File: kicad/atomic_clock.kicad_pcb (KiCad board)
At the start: 2 copper layers, 282.9 x 44.2 mm, 78 parts, among them J1 Conn_02x05_Top_Bottom, J10 Conn_02x05_Top_Bottom, J11 Conn_02x05_Top_Bottom, J12 USB_B_Micro, J13 Conn_ARM_JTAG_SWD_10, J14 Conn_01x03_Female, J2 Conn_02x05_Top_Bottom, J3 Conn_02x05_Top_Bottom, J4 Conn_02x05_Top_Bottom, J5 USB_B_Micro, J6 Conn_02x05_Top_Bottom, J7 Conn_02x05_Top_Bottom, J8 Conn_02x05_Top_Bottom, J9 Conn_02x05_Top_Bottom, Q1 Q_Dual_PMOS, Q2 Q_Dual_PMOS, SW1 SW_Push, U1 D198K, U10 ATSAMDA1E16B-A, U11 D198K, U12 D198K, U13 D198K, U14 D198K, U15 D198K, U16 MAX7221xWG, U17 D198K, U18 D198K, U19 D198K, U2 D198K, U20 NCP1117LPST33T3G, U21 mems_osc_st1630, U22 DHT20, U23 DCF77, U24 MCP73831-2-OT, U25 TXB0101, U3 D198K, U4 D198K, U5 MAX7221xWG, U6 D198K, U7 D198K, U8 D198K, U9 D198K

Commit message: Added silkscreen commentary
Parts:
- moved BT1 11.6 mm to (196.9, 110.4)
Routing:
- net Net-(BT1-Pad1): track 115.7 -> 157.1 mm
- net GND: track 489.2 -> 477.6 mm
- net /1A2: track 154.0 -> 156.3 mm
- net /DCF_PDN: track 157.8 -> 159.6 mm
- net /1B2: track 154.0 -> 154.9 mm
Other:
- board text added: "Batt full Charging"
- board text added: "DCF77 Radio controlled clock v1.0, June 2022 Erik van Zijst <erik.van.zijst@gmail.com> github.com/erikvanzijst/radioclock"
- board text added: "◯ ◉"

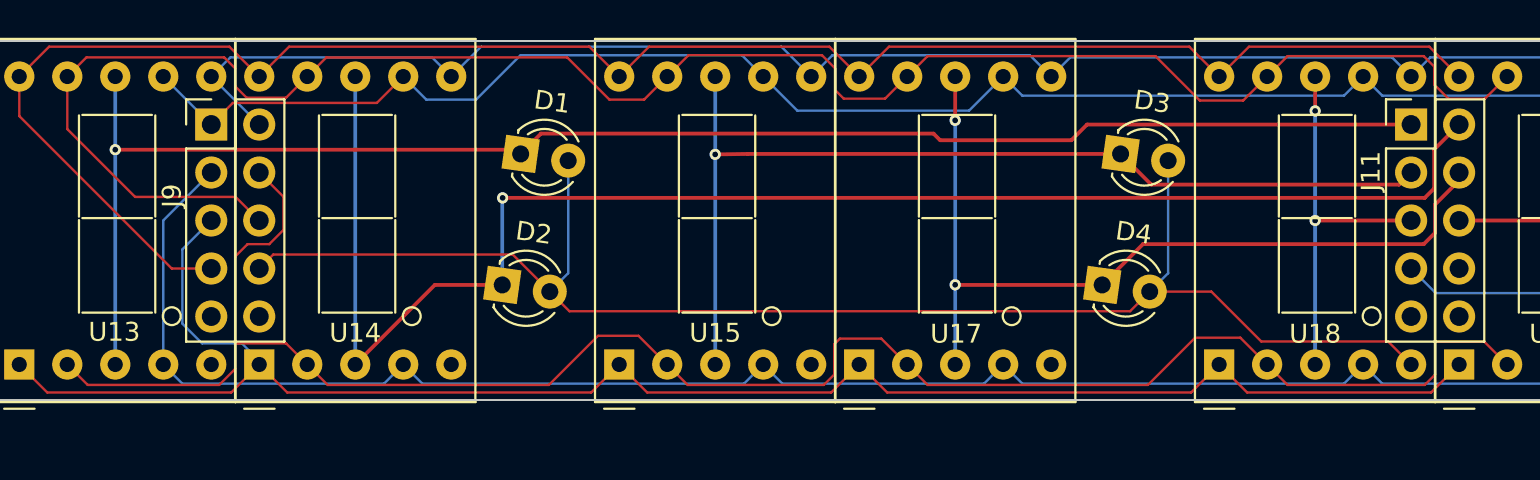
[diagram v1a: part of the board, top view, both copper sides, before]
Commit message: Switched flat top LEDs
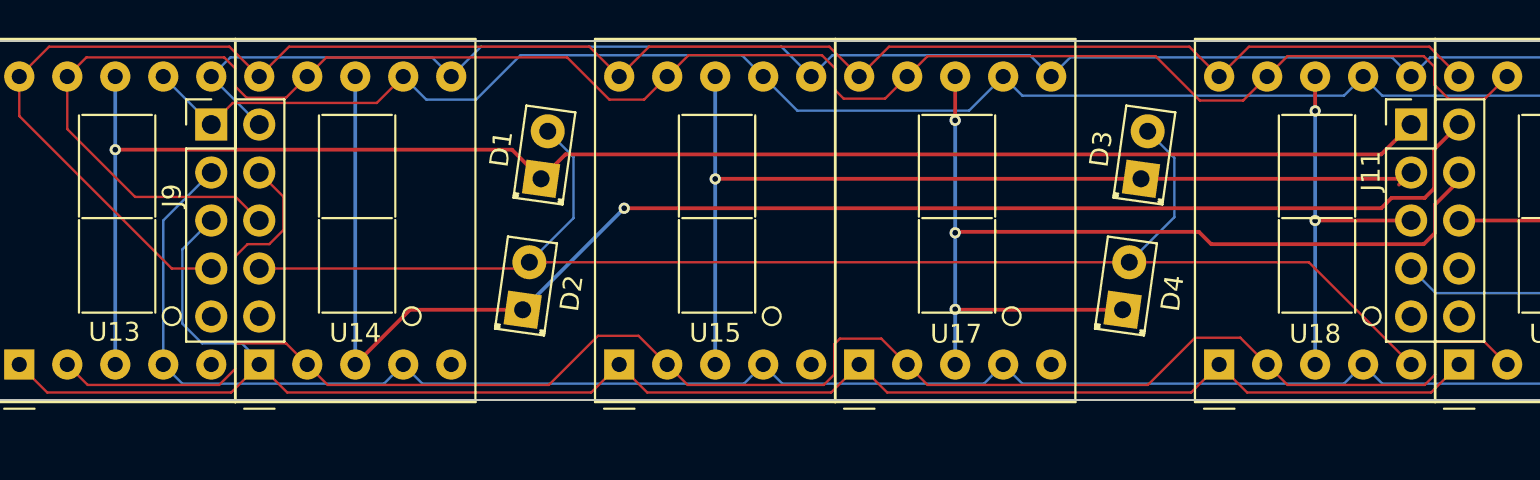
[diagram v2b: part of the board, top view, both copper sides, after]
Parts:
- D1, D2, D3, D4: footprint LED_THT:LED_D3.0mm_FlatTop -> local_footprints:LED_D2.0mm_W4.8mm_H2.5mm_FlatTop
- moved D3 1.26 mm to (277.5, 87.5), turned to 82 degrees
- moved D1 1.26 mm to (245.8, 87.5), turned to 82 degrees
- moved D2 1.26 mm to (244.8, 94.4), turned to 82 degrees
- moved D4 1.26 mm to (276.6, 94.4), turned to 82 degrees
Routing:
- net /3s13: track 45.5 -> 53.8 mm, vias 2 -> 3
- net /3s11: track 82.8 -> 80.1 mm
- net /3DP2: track 79.2 -> 80.3 mm
- net /3s10: track 84.8 -> 85.6 mm

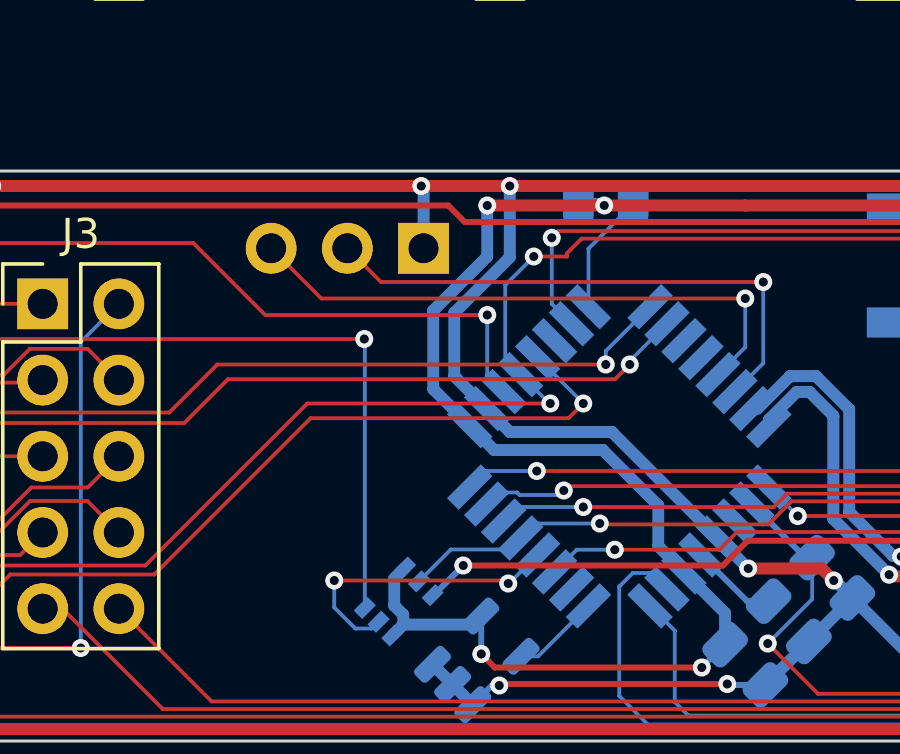
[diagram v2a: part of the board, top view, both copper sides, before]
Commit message: Placed and routed decoupling cap on VDDANA
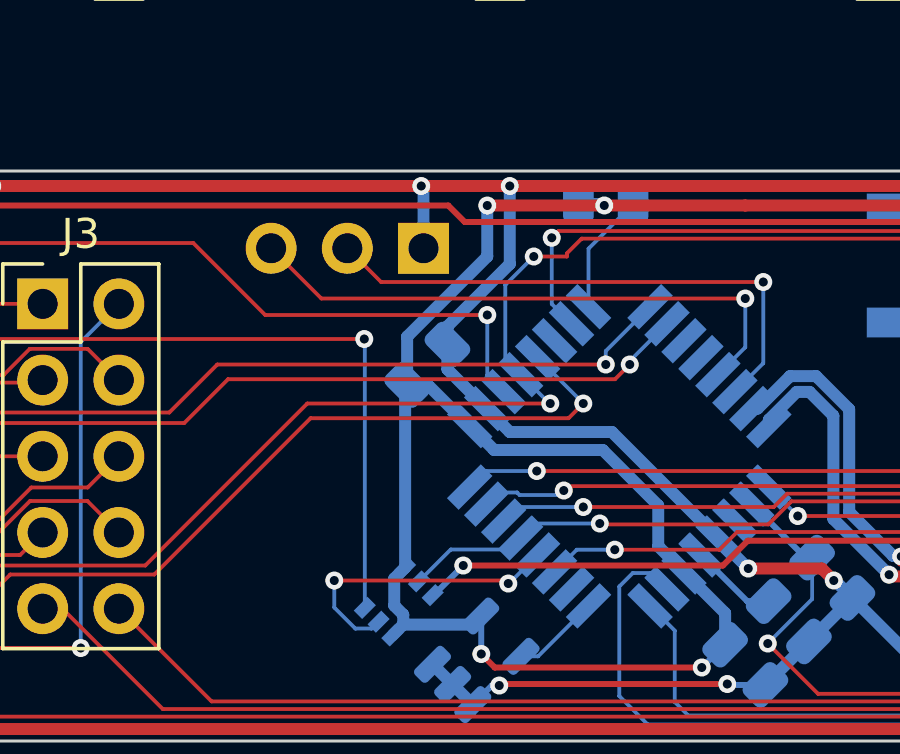
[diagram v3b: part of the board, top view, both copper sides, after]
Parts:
- added C11: 10uF CL21A106KPFNNNF, Capacitor_SMD:C_0805_2012Metric, B.Cu at (97.8, 113.1)
- BT1: value Battery_Cell -> Varta CP1654 A3
- C1, C6, C7, C8: value 100nF -> 100nF 885012207016
- C10, C9: value 4.7uF -> 4.7uF CL21A475KPFNNNE
- C2, C3: value 10uF -> 10uF CL21A106KPFNNNF
- C4: value C -> 100nF 885012207016
- C5: value C -> 1uF 885012207051
- D1, D2, D3, D4: value LED -> LED LTL-1224A
- D5, D6, D8, D9: value D -> Diode S1M-13-F
- D7: value LED -> LED HSMS-C150
- J12: value USB_B_Micro -> USB_B_Micro 10118194-0001LF
- J13: value Conn_ARM_JTAG_SWD_10 -> ARM_JTAG_SWD_10 3220-10-0100-00
- J5: value USB_B_Micro -> USB_B_Micro 1051330001
- R6: value R_Photo -> LDR NSL-19M51
- R8: value 330R -> 470R
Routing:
- net /3.3V: track 128.3 -> 135.6 mm
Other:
- board text added: "UART (3.3V)"
- board text removed: "UART"

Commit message: Added general indicator LED
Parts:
- added D10: LED HSMS-C150, LED_SMD:LED_1206_3216Metric_Pad1.42x1.75mm_HandSolder, F.Cu at (164.1, 123.8)
- added REF**: MountingHole_2.2mm_M2, MountingHole:MountingHole_2.2mm_M2, F.Cu at (300.7, 87.2)
- added REF**: OSHW-Logo_5.7x6mm_SilkScreen, Symbol:OSHW-Logo_5.7x6mm_SilkScreen, B.Cu at (94.8, 91.0)
- added REF**: OSHW-Logo_5.7x6mm_SilkScreen, Symbol:OSHW-Logo_5.7x6mm_SilkScreen, B.Cu at (237.8, 91.0)
- added REF**: MountingHole_2.2mm_M2, MountingHole:MountingHole_2.2mm_M2, F.Cu at (27.7, 94.8)
- added REF**: MountingHole_2.2mm_M2, MountingHole:MountingHole_2.2mm_M2, F.Cu at (27.6, 112.4)
- added REF**: MountingHole_2.2mm_M2, MountingHole:MountingHole_2.2mm_M2, F.Cu at (300.8, 120.0)
- added REF**: MountingHole_2.2mm_M2, MountingHole:MountingHole_2.2mm_M2, F.Cu at (27.7, 87.2)
- added REF**: MountingHole_2.2mm_M2, MountingHole:MountingHole_2.2mm_M2, F.Cu at (300.8, 112.4)
- added REF**: MountingHole_2.2mm_M2, MountingHole:MountingHole_2.2mm_M2, F.Cu at (27.6, 120.0)
- added REF**: MountingHole_2.2mm_M2, MountingHole:MountingHole_2.2mm_M2, F.Cu at (300.7, 94.8)
- added REF**: OSHW-Logo_5.7x6mm_SilkScreen, Symbol:OSHW-Logo_5.7x6mm_SilkScreen, B.Cu at (188.9, 119.4)
- moved R16 173.8 mm to (124.2, 116.7), turned to 180 degrees
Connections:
- J10 pad 7: /1IND -> unconnected-(J10-Pad7)
- J11 pad 7: /3IND -> unconnected-(J11-Pad7)
- R16 pad 2: /1IND -> /INDICATOR
- U10 pad 15: Net-(R16-Pad1) -> /INDICATOR
- U19 pad 5: /3IND -> /3DP2
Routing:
- net Net-(R16-Pad1): track 206.5 -> 40.4 mm, vias 2 -> 3
- net /INDICATOR: track 0.00 -> 22.7 mm, vias 0 -> 2
- net /3IND: track 14.8 -> 0.00 mm
- net /3DP2: track 80.3 -> 94.1 mm
- net /1IND: track 7.05 -> 0.00 mm, vias 1 -> 0
- net /2G1: track 112.8 -> 115.0 mm
- net GND: track 477.8 -> 480.0 mm
- net /DCF_PDN: track 159.6 -> 158.8 mm
- net /DCF_DATA: track 161.7 -> 161.0 mm
- net /2s0: track 72.2 -> 71.6 mm
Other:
- board text added: "DHT20"
- board text added: "MAS DAEV6180B1COB.005 Time signal receiver module"
- board text added: "MAX7221"
- board text added: "PCB A"
- board text added: "PCB B"
- board text added: "PCB C"
- board text added: "Radio Controlled Clock Syncing to DCF77, Germany v1.0, June 2022 Erik van Zijst github.com/erikvanzijst/radioclock"
- board text added: "Radio Controlled Clock Syncing to DCF77, Mainflingen, Germany v1.0, June 2022 Erik van Zijst <erik.van.zijst@gmail.com> github.com/erikvanzijst/radioclock"
- board text added: "SAMDA1E"
- board text added: "TOP"
- board text removed: "DCF77 Radio controlled clock v1.0, June 2022 Erik van Zijst <erik.van.zijst@gmail.com> github.com/erikvanzijst/radioclock"

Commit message: Getting ready for v1.0
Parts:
- moved D1 1.19 mm to (245.8, 88.7)
- moved D2 1.19 mm to (244.8, 95.6)
- moved D3 1.19 mm to (277.5, 88.7)
- moved D4 1.19 mm to (276.6, 95.6)
- moved J11 1.19 mm to (291.7, 87.1)
- moved J2 1.19 mm to (34.2, 87.1)
- moved J4 1.19 mm to (85.0, 87.1)
- moved J7 1.19 mm to (135.8, 87.1)
- moved J9 1.19 mm to (228.2, 87.1)
- moved REF** 1.19 mm to (300.7, 88.4)
- moved REF** 1.19 mm to (94.8, 92.2)
- moved REF** 1.19 mm to (237.8, 92.2)
- moved REF** 1.19 mm to (27.7, 96.0)
- moved REF** 1.19 mm to (27.7, 88.4)
- moved REF** 1.19 mm to (300.7, 96.0)
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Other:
- board size 282.9 x 44.2 mm -> 282.7 x 43 mm
- board text added: "JLCJLCJLCJLC"

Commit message: Version 1.0 for submission to JLCPCB
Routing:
- net /2F1: track 117.6 -> 116.6 mm
- net /3s12: track 53.1 -> 52.2 mm
- net /2s9: track 72.1 -> 72.7 mm

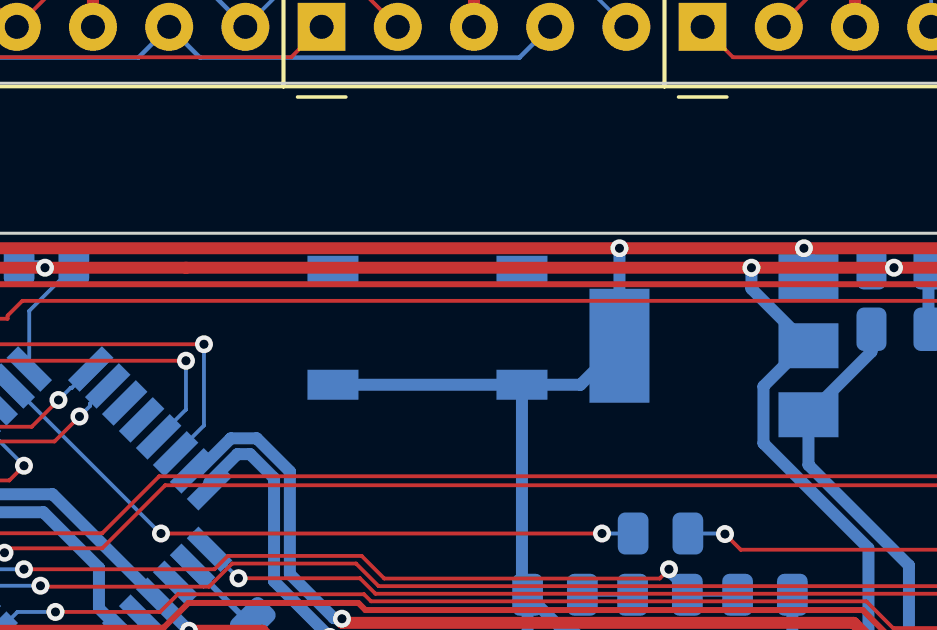
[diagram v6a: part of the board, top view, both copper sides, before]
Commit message: Fix short circuit in LDO symbol and footprint
The heatsink on the NCP1117LP LDO was incorrectly wired to GND, while
this pin is actually connected to Vout, causing a short circuit on
the assembled board.

https://twitter.com/erikvanzijst/status/1541097400571420672
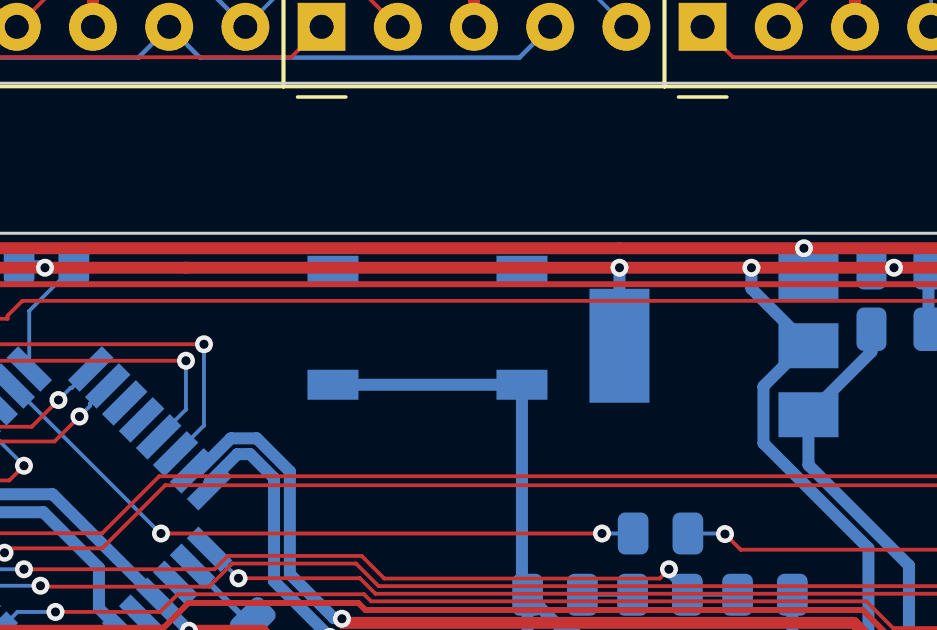
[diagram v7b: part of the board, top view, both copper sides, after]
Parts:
- removed the REF** at (94.8, 92.2)
- removed the REF** at (237.8, 92.2)
- removed the REF** at (188.9, 119.4)
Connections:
- U20 pad 4: GND -> /3.3V
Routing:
- net GND: track 480.0 -> 473.0 mm, vias 20 -> 19
- net /3.3V: track 135.6 -> 138.2 mm, vias 9 -> 10
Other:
- board text added: "Radio Controlled Clock Syncing to DCF77, Germany v1.1, June 2022 Erik van Zijst github.com/erikvanzijst/radioclock"
- board text added: "Radio Controlled Clock Syncing to DCF77, Mainflingen, Germany v1.1, June 2022 Erik van Zijst <erik.van.zijst@gmail.com> github.com/erikvanzijst/radioclock"
- board text removed: "Radio Controlled Clock Syncing to DCF77, Germany v1.0, June 2022 Erik van Zijst github.com/erikvanzijst/radioclock"
- board text removed: "Radio Controlled Clock Syncing to DCF77, Mainflingen, Germany v1.0, June 2022 Erik van Zijst <erik.van.zijst@gmail.com> github.com/erikvanzijst/radioclock"

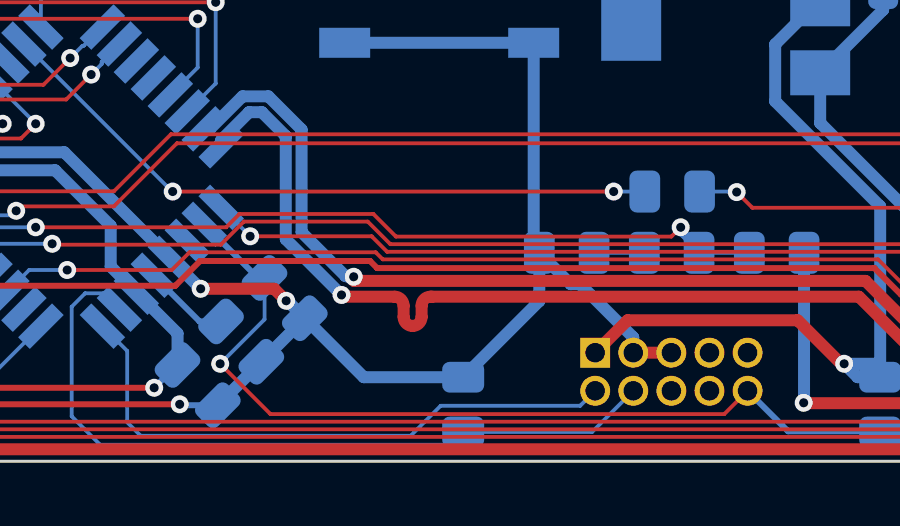
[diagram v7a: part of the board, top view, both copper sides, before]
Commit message: Fix pull-up resistor on SWCLK
See https://twitter.com/erikvanzijst/status/1541787726684585988
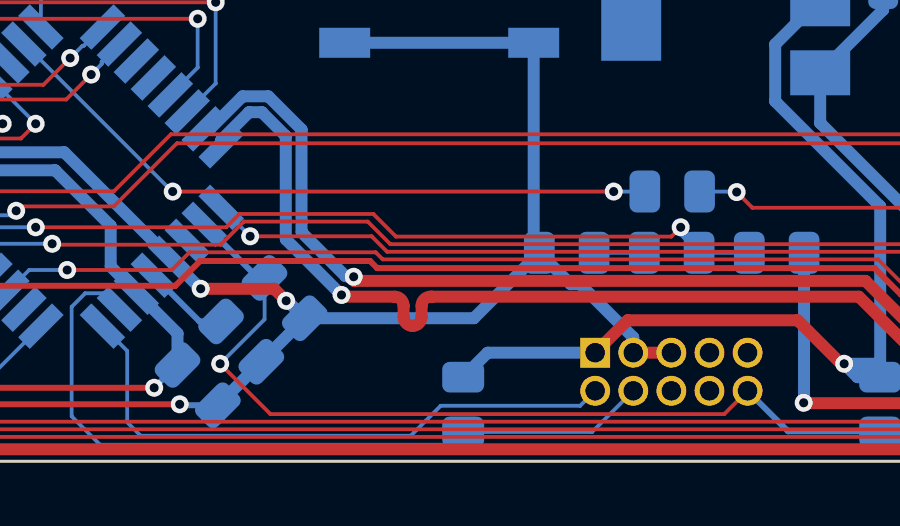
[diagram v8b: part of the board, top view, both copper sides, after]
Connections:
- R2 pad 2: GND -> /3.3V
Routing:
- net /3.3V: track 138.2 -> 142.9 mm
- net GND: track 473.0 -> 470.4 mm
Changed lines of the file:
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@@
       (net 46 "/SWCLK") (pintype "passive"))
     (pad "2" smd roundrect (at 0.9125 0 90) (size 1.025 1.4) (layers "B.Cu" "B.Paste" "B.Mask") (roundrect_rratio 0.243902439)
-      (net 3 "GND") (pintype "passive"))
+      (net 10 "/3.3V") (pintype "passive"))
     (model "${KICAD6_3DMODEL_DIR}/Resistor_SMD.3dshapes/R_0805_2012Metric.wrl"
       (offset (xyz 0 0 0))
@@
   (via (at 83.2835 107.174) (size 0.6) (drill 0.3) (layers "F.Cu" "B.Cu") (net 3))
   (via (at 97.5825 107.174) (size 0.6) (drill 0.3) (layers "F.Cu" "B.Cu") (net 3))
-  (segment (start 119.7705 120.334) (end 117.233 122.8715) (width 0.4) (layer "B.Cu") (net 3))
   (segment (start 241.883 122.224) (end 240.553767 122.224) (width 0.4) (layer "B.Cu") (net 3))
   (segment (start 99.936502 123.824) (end 99.300417 124.460085) (width 0.2) (layer "B.Cu") (net 3))
@@
   (segment (start 283.863147 114.475613) (end 283.863147 119.004147) (width 0.4) (layer "B.Cu") (net 3))
   (segment (start 109.054751 123.805751) (end 107.814751 123.805751) (width 0.2) (layer "B.Cu") (net 3))
-  (segment (start 119.7705 118.724) (end 119.7705 120.334) (width 0.4) (layer "B.Cu") (net 3))
   (segment (start 237.5955 111.824) (end 238.265387 111.824) (width 0.4) (layer "B.Cu") (net 3))
   (segment (start 56.953222 112.909) (end 55.968 112.909) (width 0.4) (layer "B.Cu") (net 3))
@@
   (segment (start 141.783 107.1735) (end 141.783 115.374) (width 0.4) (layer "B.Cu") (net 3))
   (segment (start 284.518 119.659) (end 285.491187 119.659) (width 0.4) (layer "B.Cu") (net 3))
+  (segment (start 117.588749 120.905751) (end 119.7705 118.724) (width 0.4) (layer "B.Cu") (net 3))
   (segment (start 241.983 112.774) (end 242.283 113.074) (width 0.4) (layer "B.Cu") (net 3))
   (segment (start 98.454751 111.850677) (end 100.5325 109.772928) (width 0.4) (layer "B.Cu") (net 3))
@@
   (segment (start 120.82002 119.77352) (end 121.13252 119.77352) (width 0.4) (layer "B.Cu") (net 3))
   (segment (start 54.583 118.824) (end 55.018 119.259) (width 0.4) (layer "B.Cu") (net 3))
-  (segment (start 113.9205 122.8715) (end 111.954751 120.905751) (width 0.4) (layer "B.Cu") (net 3))
   (segment (start 162.883 121.524) (end 162.883 123.924) (width 0.4) (layer "B.Cu") (net 3))
   (segment (start 110.504751 122.355751) (end 111.954751 120.905751) (width 0.4) (layer "B.Cu") (net 3))
@@
   (segment (start 283.433 107.1735) (end 283.433 111.71224) (width 0.4) (layer "B.Cu") (net 3))
   (segment (start 241.983 112.774) (end 241.033 111.824) (width 0.4) (layer "B.Cu") (net 3))
+  (segment (start 111.954751 120.905751) (end 117.588749 120.905751) (width 0.4) (layer "B.Cu") (net 3))
   (segment (start 82.723 107.734) (end 83.2835 107.1735) (width 0.4) (layer "B.Cu") (net 3))
   (segment (start 141.783 115.374) (end 142.083 115.674) (width 0.4) (layer "B.Cu") (net 3))
@@
   (segment (start 273.683 113.624) (end 273.683 107.274) (width 0.4) (layer "B.Cu") (net 3))
   (segment (start 165.083 124.224) (end 167.583 124.224) (width 0.4) (layer "B.Cu") (net 3))
-  (segment (start 117.233 122.8715) (end 113.9205 122.8715) (width 0.4) (layer "B.Cu") (net 3))
   (segment (start 97.658 107.249) (end 97.5825 107.1735) (width 0.4) (layer "B.Cu") (net 3))
   (segment (start 81.883 107.734) (end 82.723 107.734) (width 0.4) (layer "B.Cu") (net 3))
@@
   (segment (start 97.045132 119.892629) (end 96.683 120.254761) (width 0.4) (layer "B.Cu") (net 10))
   (segment (start 96.983 121.793239) (end 96.620868 122.155371) (width 0.4) (layer "B.Cu") (net 10))
+  (segment (start 118.0505 122.054) (end 121.633 122.054) (width 0.4) (layer "B.Cu") (net 10))
   (segment (start 96.683 121.162586) (end 96.983 121.462586) (width 0.4) (layer "B.Cu") (net 10))
   (segment (start 131.983 107.824) (end 131.984 107.823) (width 0.4) (layer "B.Cu") (net 10))
@@
   (segment (start 99.565583 121.507915) (end 99.280259 121.793239) (width 0.4) (layer "B.Cu") (net 10))
   (segment (start 129.933 122.424) (end 131.133 122.424) (width 0.4) (layer "B.Cu") (net 10))
+  (segment (start 117.233 122.8715) (end 118.0505 122.054) (width 0.4) (layer "B.Cu") (net 10))
   (segment (start 48.389989 100.806811) (end 49.403 99.7938) (width 0.127) (layer "F.Cu") (net 11))
   (segment (start 75.9242 100.915) (end 86.3818 100.915) (width 0.127) (layer "F.Cu") (net 11))
